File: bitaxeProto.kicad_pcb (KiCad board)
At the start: 6 copper layers, 76 x 101 mm, 214 parts, among them J1 XT30, J4 Conn_01x04, J5 Conn_01x10, J6 USB_C_Receptacle_USB2.0, J8 TC2030-IDC, Q1 BSS138, SW3 SWITCH-SPST, SW4 SWITCH-SPST, U12 ESP32-S3-WROOM-1, U13 TS3011, U14 SN74AVC2T45DCUR, U15 25MHz, U16 TLV75512PDQNR, U17 TLV755075PDQNR, U18 TLV75512PDQNR, U19 TLV3542, U2 TPS546D24SRVFR, U3 TLV755075PDQNR, U4 TPS62933DRLR, U5 TPS62933DRLR, U8 25MHz, U9 TPS22919DCKR

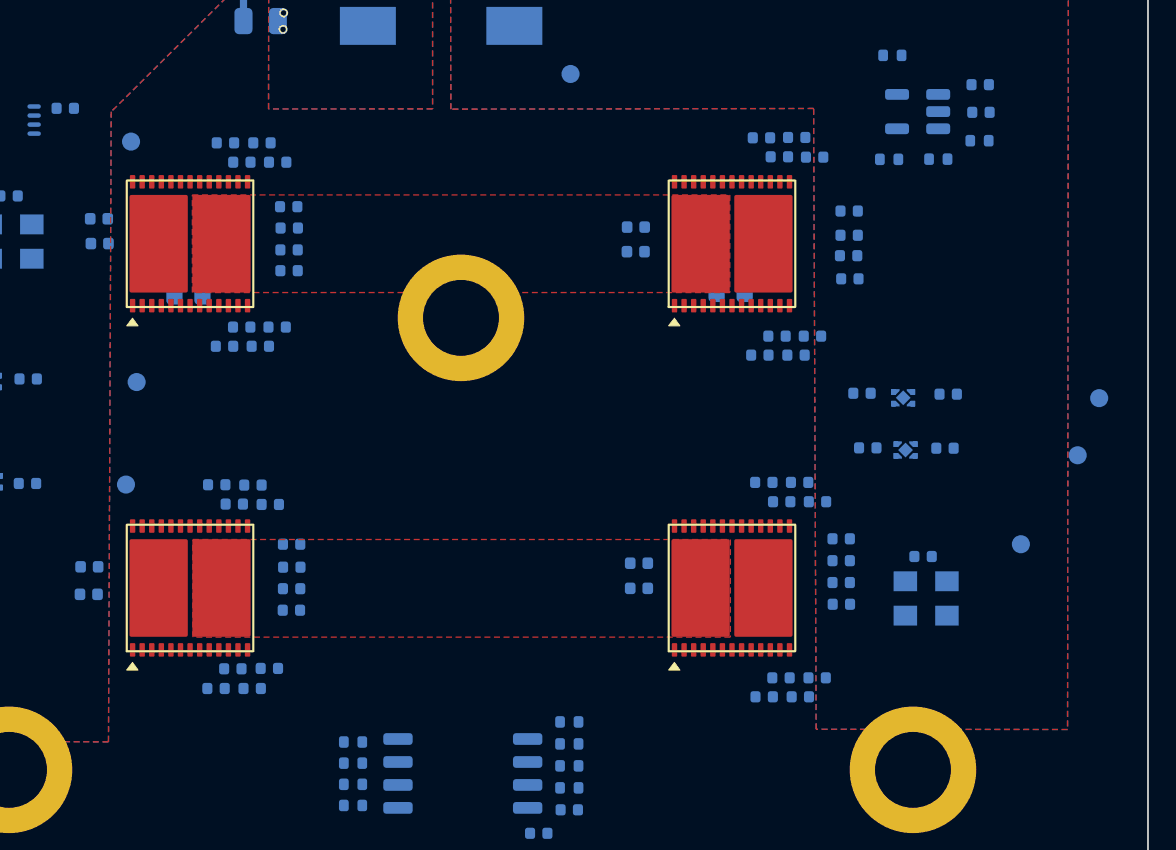
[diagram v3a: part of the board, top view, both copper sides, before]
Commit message: power plane tweaking
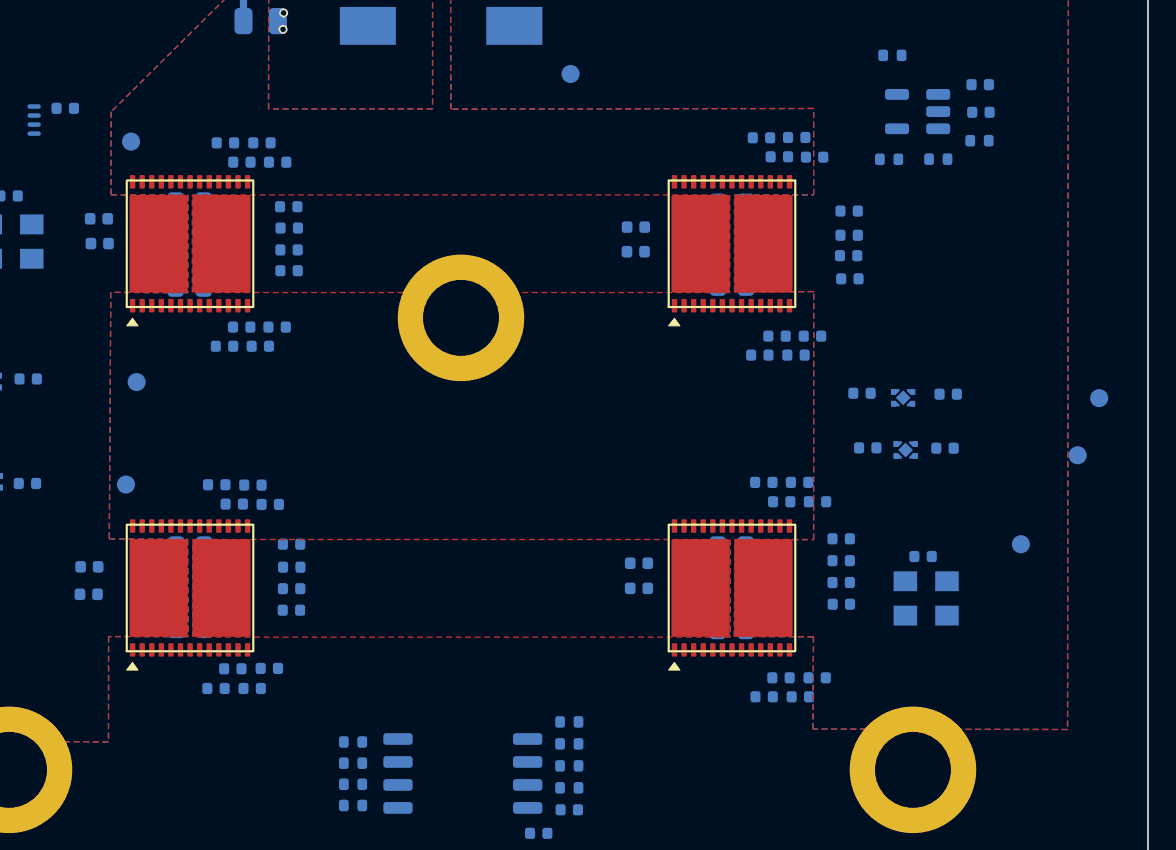
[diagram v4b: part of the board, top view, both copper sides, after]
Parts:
- moved C75 2.65 mm to (116.0, 124.6)
- moved C67 2.65 mm to (146.0, 124.6)
- moved C66 2.09 mm to (146.0, 129.3)
- moved C78 2.03 mm to (116.0, 129.2)
- moved C73 1.09 mm to (116.0, 126.1)
- moved C68 1.07 mm to (146.0, 126.1)
- moved C69 0.51 mm to (146.0, 127.7)
- moved C74 0.47 mm to (116.0, 127.7)
- moved C81 0.47 mm to (116.0, 107.1)
- moved C82 0.46 mm to (116.0, 108.8)
- moved C83 0.43 mm to (116.0, 110.4)
- moved C80 0.43 mm to (116.0, 105.5)
- moved C93 0.37 mm to (146.0, 108.7)
- moved C71 0.35 mm to (146.0, 107.2)
- moved C95 0.35 mm to (146.0, 110.3)
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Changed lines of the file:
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@@
 	(footprint "Capacitor_SMD:C_0603_1608Metric"
 		(layer "B.Cu")
-		(at 145.915 110.65 180)
+		(at 145.99 110.31 180)
 		(descr "Capacitor SMD 0603 (1608 Metric), square (rectangular) end terminal, IPC-7351 nominal, (Body size source: IPC-SM-782 page 76, https://www.pcb-3d.com/wordpress/wp-content/uploads/ipc-sm-782a_amendment_1_and_2.pdf)")
 		(tags "capacitor")
@@
 	(footprint "Capacitor_SMD:C_0603_1608Metric"
 		(layer "B.Cu")
-		(at 115.985 105.96 180)
+		(at 115.99 105.53 180)
 		(descr "Capacitor SMD 0603 (1608 Metric), square (rectangular) end terminal, IPC-7351 nominal, (Body size source: IPC-SM-782 page 76, https://www.pcb-3d.com/wordpress/wp-content/uploads/ipc-sm-782a_amendment_1_and_2.pdf)")
 		(tags "capacitor")
@@
 	(footprint "Capacitor_SMD:C_0603_1608Metric"
 		(layer "B.Cu")
-		(at 115.945 127.2115 180)
+		(at 116.02 124.56 180)
 		(descr "Capacitor SMD 0603 (1608 Metric), square (rectangular) end terminal, IPC-7351 nominal, (Body size source: IPC-SM-782 page 76, https://www.pcb-3d.com/wordpress/wp-content/uploads/ipc-sm-782a_amendment_1_and_2.pdf)")
 		(tags "capacitor")
@@
 	(footprint "Capacitor_SMD:C_0603_1608Metric"
 		(layer "B.Cu")
-		(at 145.975 127.2115 180)
+		(at 145.975 124.56 180)
 		(descr "Capacitor SMD 0603 (1608 Metric), square (rectangular) end terminal, IPC-7351 nominal, (Body size source: IPC-SM-782 page 76, https://www.pcb-3d.com/wordpress/wp-content/uploads/ipc-sm-782a_amendment_1_and_2.pdf)")
 		(tags "capacitor")
@@
 	(footprint "Capacitor_SMD:C_0603_1608Metric"
 		(layer "B.Cu")
-		(at 115.975 107.61 180)
+		(at 115.99 107.14 180)
 		(descr "Capacitor SMD 0603 (1608 Metric), square (rectangular) end terminal, IPC-7351 nominal, (Body size source: IPC-SM-782 page 76, https://www.pcb-3d.com/wordpress/wp-content/uploads/ipc-sm-782a_amendment_1_and_2.pdf)")
 		(tags "capacitor")
@@
 	(footprint "Capacitor_SMD:C_0603_1608Metric"
 		(layer "B.Cu")
-		(at 115.955 109.21 180)
+		(at 115.99 108.75 180)
 		(descr "Capacitor SMD 0603 (1608 Metric), square (rectangular) end terminal, IPC-7351 nominal, (Body size source: IPC-SM-782 page 76, https://www.pcb-3d.com/wordpress/wp-content/uploads/ipc-sm-782a_amendment_1_and_2.pdf)")
 		(tags "capacitor")
@@
 	(footprint "Capacitor_SMD:C_0603_1608Metric"
 		(layer "B.Cu")
-		(at 145.965 127.2115 180)
+		(at 145.975 126.14 180)
 		(descr "Capacitor SMD 0603 (1608 Metric), square (rectangular) end terminal, IPC-7351 nominal, (Body size source: IPC-SM-782 page 76, https://www.pcb-3d.com/wordpress/wp-content/uploads/ipc-sm-782a_amendment_1_and_2.pdf)")
 		(tags "capacitor")
@@
 	(footprint "Capacitor_SMD:C_0603_1608Metric"
 		(layer "B.Cu")
-		(at 145.965 127.2115 180)
+		(at 145.975 129.3 180)
 		(descr "Capacitor SMD 0603 (1608 Metric), square (rectangular) end terminal, IPC-7351 nominal, (Body size source: IPC-SM-782 page 76, https://www.pcb-3d.com/wordpress/wp-content/uploads/ipc-sm-782a_amendment_1_and_2.pdf)")
 		(tags "capacitor")
@@
 	(footprint "Capacitor_SMD:C_0603_1608Metric"
 		(layer "B.Cu")
-		(at 145.965 127.2115 180)
+		(at 145.975 127.72 180)
 		(descr "Capacitor SMD 0603 (1608 Metric), square (rectangular) end terminal, IPC-7351 nominal, (Body size source: IPC-SM-782 page 76, https://www.pcb-3d.com/wordpress/wp-content/uploads/ipc-sm-782a_amendment_1_and_2.pdf)")
 		(tags "capacitor")
@@
 	(footprint "Capacitor_SMD:C_0603_1608Metric"
 		(layer "B.Cu")
-		(at 145.985 107.52 180)
+		(at 145.99 107.17 180)
 		(descr "Capacitor SMD 0603 (1608 Metric), square (rectangular) end terminal, IPC-7351 nominal, (Body size source: IPC-SM-782 page 76, https://www.pcb-3d.com/wordpress/wp-content/uploads/ipc-sm-782a_amendment_1_and_2.pdf)")
 		(tags "capacitor")
@@
 	(footprint "Capacitor_SMD:C_0603_1608Metric"
 		(layer "B.Cu")
-		(at 115.95 127.2115 180)
+		(at 116.02 126.12 180)
 		(descr "Capacitor SMD 0603 (1608 Metric), square (rectangular) end terminal, IPC-7351 nominal, (Body size source: IPC-SM-782 page 76, https://www.pcb-3d.com/wordpress/wp-content/uploads/ipc-sm-782a_amendment_1_and_2.pdf)")
 		(tags "capacitor")
@@
 	(footprint "Capacitor_SMD:C_0603_1608Metric"
 		(layer "B.Cu")
-		(at 115.965 127.2115 180)
+		(at 116.02 127.68 180)
 		(descr "Capacitor SMD 0603 (1608 Metric), square (rectangular) end terminal, IPC-7351 nominal, (Body size source: IPC-SM-782 page 76, https://www.pcb-3d.com/wordpress/wp-content/uploads/ipc-sm-782a_amendment_1_and_2.pdf)")
 		(tags "capacitor")
@@
 	(footprint "Capacitor_SMD:C_0603_1608Metric"
 		(layer "B.Cu")
-		(at 145.905 109.1 180)
+		(at 145.99 108.74 180)
 		(descr "Capacitor SMD 0603 (1608 Metric), square (rectangular) end terminal, IPC-7351 nominal, (Body size source: IPC-SM-782 page 76, https://www.pcb-3d.com/wordpress/wp-content/uploads/ipc-sm-782a_amendment_1_and_2.pdf)")
 		(tags "capacitor")
@@
 	(footprint "Capacitor_SMD:C_0603_1608Metric"
 		(layer "B.Cu")
-		(at 115.945 127.2115 180)
+		(at 116.02 129.24 180)
 		(descr "Capacitor SMD 0603 (1608 Metric), square (rectangular) end terminal, IPC-7351 nominal, (Body size source: IPC-SM-782 page 76, https://www.pcb-3d.com/wordpress/wp-content/uploads/ipc-sm-782a_amendment_1_and_2.pdf)")
 		(tags "capacitor")
@@
 	(footprint "Capacitor_SMD:C_0603_1608Metric"
 		(layer "B.Cu")
-		(at 115.925 110.79 180)
+		(at 115.99 110.36 180)
 		(descr "Capacitor SMD 0603 (1608 Metric), square (rectangular) end terminal, IPC-7351 nominal, (Body size source: IPC-SM-782 page 76, https://www.pcb-3d.com/wordpress/wp-content/uploads/ipc-sm-782a_amendment_1_and_2.pdf)")
 		(tags "capacitor")
@@
 	(footprint "Capacitor_SMD:C_0603_1608Metric"
 		(layer "B.Cu")
-		(at 145.975 105.94 180)
+		(at 145.99 105.6 180)
 		(descr "Capacitor SMD 0603 (1608 Metric), square (rectangular) end terminal, IPC-7351 nominal, (Body size source: IPC-SM-782 page 76, https://www.pcb-3d.com/wordpress/wp-content/uploads/ipc-sm-782a_amendment_1_and_2.pdf)")
 		(tags "capacitor")
@@
 		(polygon
 			(pts
-				(xy 118.006359 92.384555) (xy 117.99752 94.307498) (xy 111.652186 100.598093) (xy 111.501201 135.451623)
+				(xy 118.006359 92.384555) (xy 117.99752 94.307498) (xy 111.652186 100.598093) (xy 111.637242 105.196146)
+				(xy 115.9 105.21) (xy 115.889961 110.61105) (xy 111.630173 110.588952) (xy 111.547172 124.223624)
+				(xy 115.88 124.25) (xy 115.910237 129.63217) (xy 111.506942 129.627828) (xy 111.501201 135.451623)
 				(xy 97.089241 135.416852) (xy 97.060163 76.577513) (xy 119.091284 76.472361) (xy 119.108716 83.787529)
 				(xy 147.271429 83.720428) (xy 147.268567 89.742904) (xy 137.469998 89.742904) (xy 137.470004 87.486326)
@@
 			(pts
 				(xy 133.213648 90.14991) (xy 133.213741 90.169009) (xy 164.599679 90.194777) (xy 164.550304 134.769582)
-				(xy 150.644954 134.754179) (xy 150.505132 100.417572) (xy 130.440363 100.456998) (xy 130.416101 90.149966)
+				(xy 150.467396 134.744612) (xy 150.497904 129.642584) (xy 146.120934 129.616412) (xy 146.15 124.26)
+				(xy 150.504289 124.261909) (xy 150.510303 110.545636) (xy 146.13 110.57) (xy 146.13 105.2) (xy 150.506435 105.198807)
+				(xy 150.505132 100.417572) (xy 130.440363 100.456998) (xy 130.416101 90.149966)
 			)
 		)

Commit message: routing progress
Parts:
- removed FB10, FB3, FB4, FB5, FB6, FB7, FB8, FB9: FerriteBead_Small, Inductor_SMD:L_0402_1005Metric
- added U1: STHW4-DU-HN050206, bitaxeProto:PAD-SMD_L5.0-W2.0_STHW4-DU-HN050206, F.Cu at (130.2, 85.6)
- moved TP6 19.8 mm to (131.8, 121.8)
- moved C52 19.7 mm to (138.2, 132.3), turned to -90 degrees
- moved TP12 19.6 mm to (131.9, 123.9)
- moved U15 16.9 mm to (140.4, 132.2), turned to 90 degrees
- moved C54 14.9 mm to (117.7, 118.5), turned to 90 degrees
- moved C50 14.7 mm to (143.2, 116.2), turned to 90 degrees
- moved C53 14.7 mm to (117.7, 115.8), turned to -90 degrees
- moved C55 14.6 mm to (143.2, 118.3), turned to 90 degrees
- moved U18 14.5 mm to (119.2, 118.0)
- moved U17 14.3 mm to (119.2, 116.2)
- moved C57 14.2 mm to (120.9, 118.3), turned to 90 degrees
- moved U16 14.2 mm to (141.5, 118.2)
- moved U3 14.0 mm to (141.5, 116.3)
- moved C56 13.9 mm to (120.9, 116.2), turned to 90 degrees
- moved TP13 13.9 mm to (120.6, 62.4)
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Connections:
- A1 pad 21: Net-(A1-VDDIO12-Pad21) -> /ASIC/1V2
- A1 pad 22: Net-(A1-VDDH-Pad22) -> /ASIC/0V75
- A1 pad 5: Net-(A1-VDDH-Pad22) -> /ASIC/0V75
- A1 pad 6: Net-(A1-VDDIO12-Pad21) -> /ASIC/1V2
- A4 pad 21: Net-(A4-VDDIO12-Pad21) -> /ASIC/1V2-0
- A4 pad 22: Net-(A4-VDDH-Pad22) -> /ASIC/0V75-0
- A4 pad 5: Net-(A4-VDDH-Pad22) -> /ASIC/0V75-0
- A4 pad 6: Net-(A4-VDDIO12-Pad21) -> /ASIC/1V2-0
- C52 pad 1: GND -> /ASIC/GND0
- U15 pad 2: GND -> /ASIC/GND0
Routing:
- net /5V_SWITCH: track 0.00 -> 123.5 mm, vias 3 -> 5
- net /ASIC/1V2-0: track 0.00 -> 60.8 mm, vias 0 -> 5
- net /ASIC/1V2: track 0.00 -> 37.5 mm, vias 0 -> 7
- net /ASIC/Level Shifter/RST_IN: track 0.00 -> 26.0 mm, vias 0 -> 1
- net /ASIC/Level Shifter/TX_OUT: track 0.00 -> 25.1 mm, vias 0 -> 2
- net /ASIC/0V75: track 0.00 -> 23.8 mm, vias 0 -> 5
- net /ASIC/GND0: track 0.00 -> 21.0 mm, vias 0 -> 10
- net GND: track 23.6 -> 44.1 mm, vias 13 -> 33
- net /ASIC/Level Shifter/RST_OUT: track 0.00 -> 16.2 mm, vias 0 -> 2
- net /ASIC/Level Shifter/TX_IN: track 0.00 -> 15.1 mm, vias 0 -> 1
- net /ASIC/TX_2V4: track 0.00 -> 12.8 mm, vias 0 -> 1
- net Net-(A3-nRST-Pad19): track 0.00 -> 12.4 mm
- net Net-(A1-nRST-Pad7): track 0.00 -> 12.4 mm
- net Net-(A3-CLKO): track 0.00 -> 12.3 mm
- net Net-(A1-UTXP): track 0.00 -> 12.2 mm
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- added copper zone on B.Cu, net /5V
- added copper zone on B.Cu, net /ASIC/GND0
- added copper zone on In1.Cu, net /ASIC/GND0
- added copper zone on In4.Cu, net /ASIC/GND0
- added copper zone on B.Cu, net Net-(U4-SW)
- added copper zone on B.Cu, net Net-(U5-SW)
